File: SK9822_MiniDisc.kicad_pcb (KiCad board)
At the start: 4 copper layers, 220 x 220 mm, 341 parts, among them P1 CONN_01X04, P2 CONN_01X04

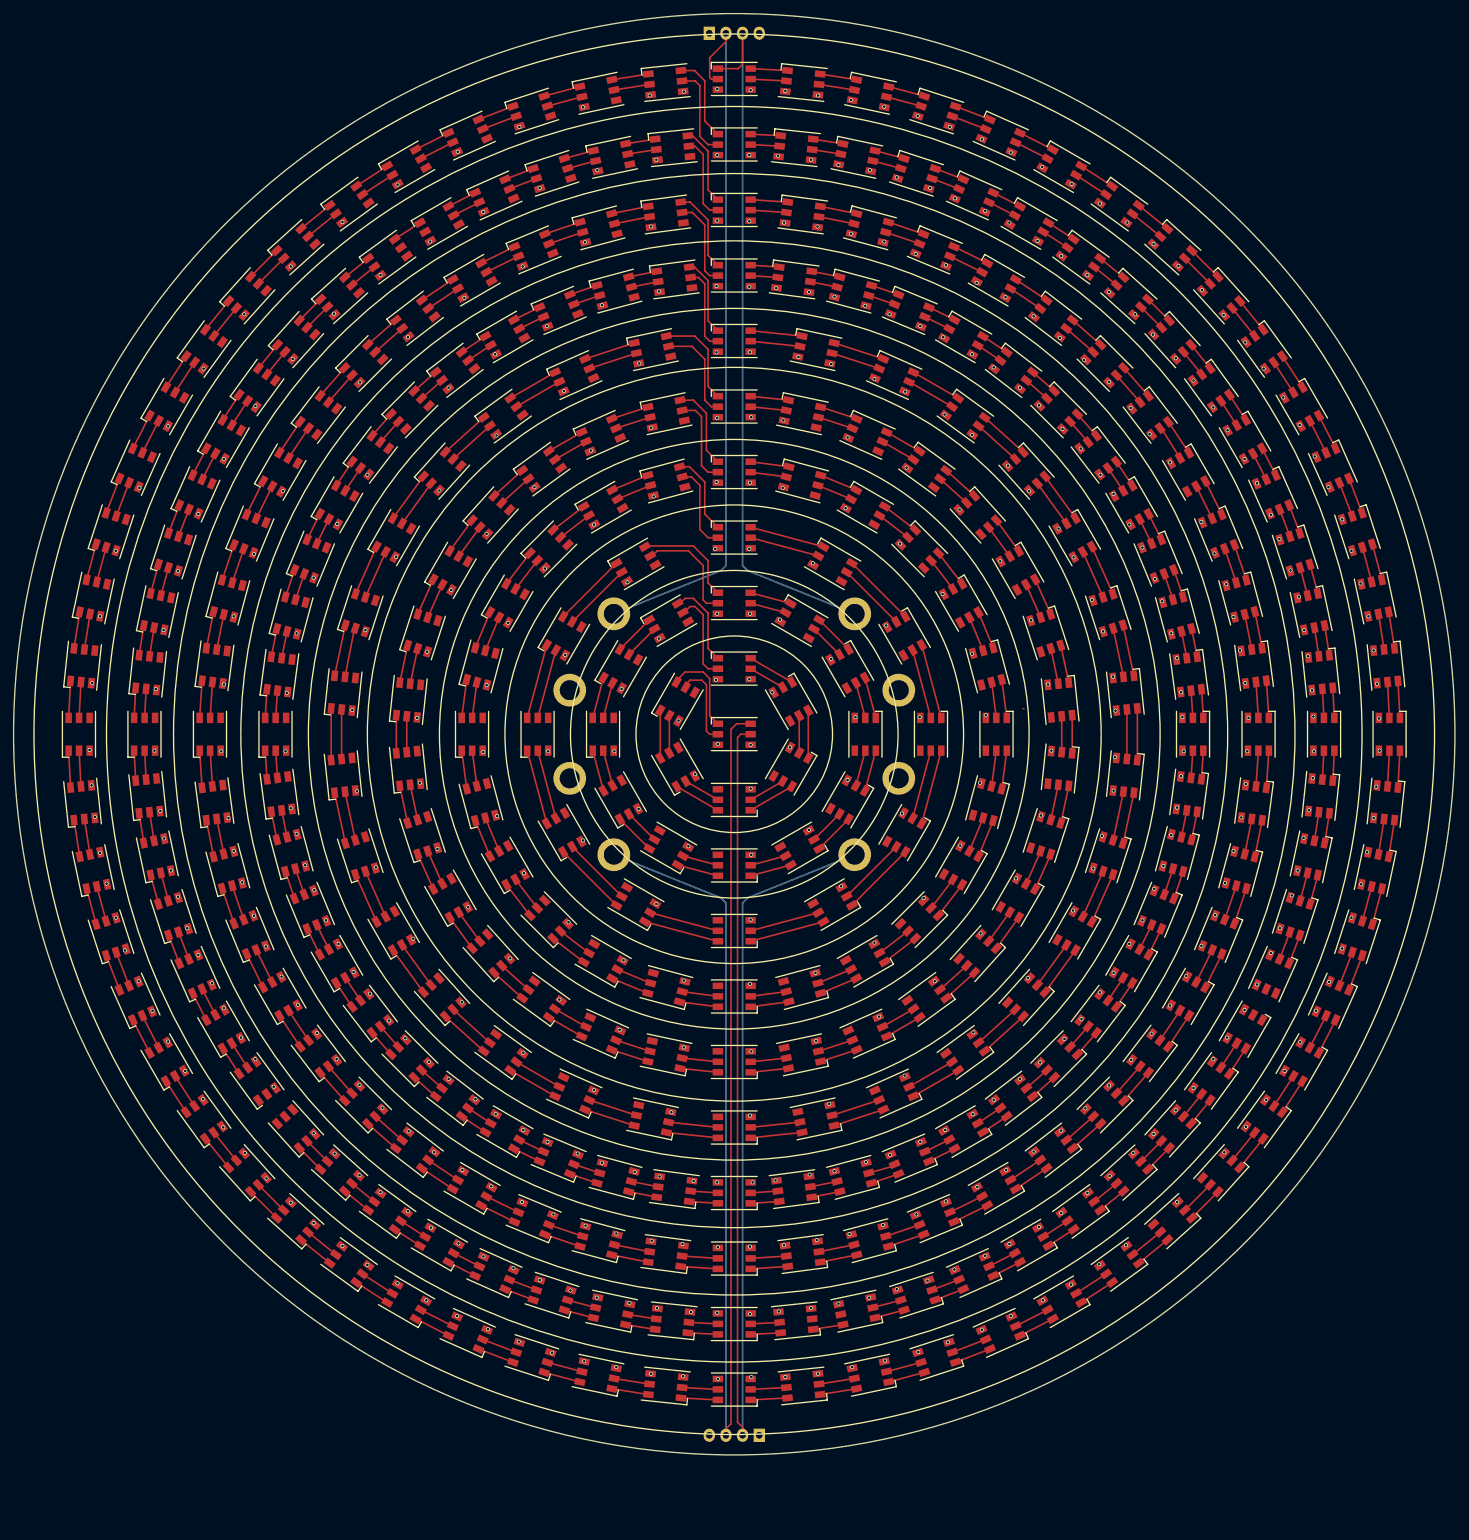
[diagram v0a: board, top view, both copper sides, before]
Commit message: full gnd layout
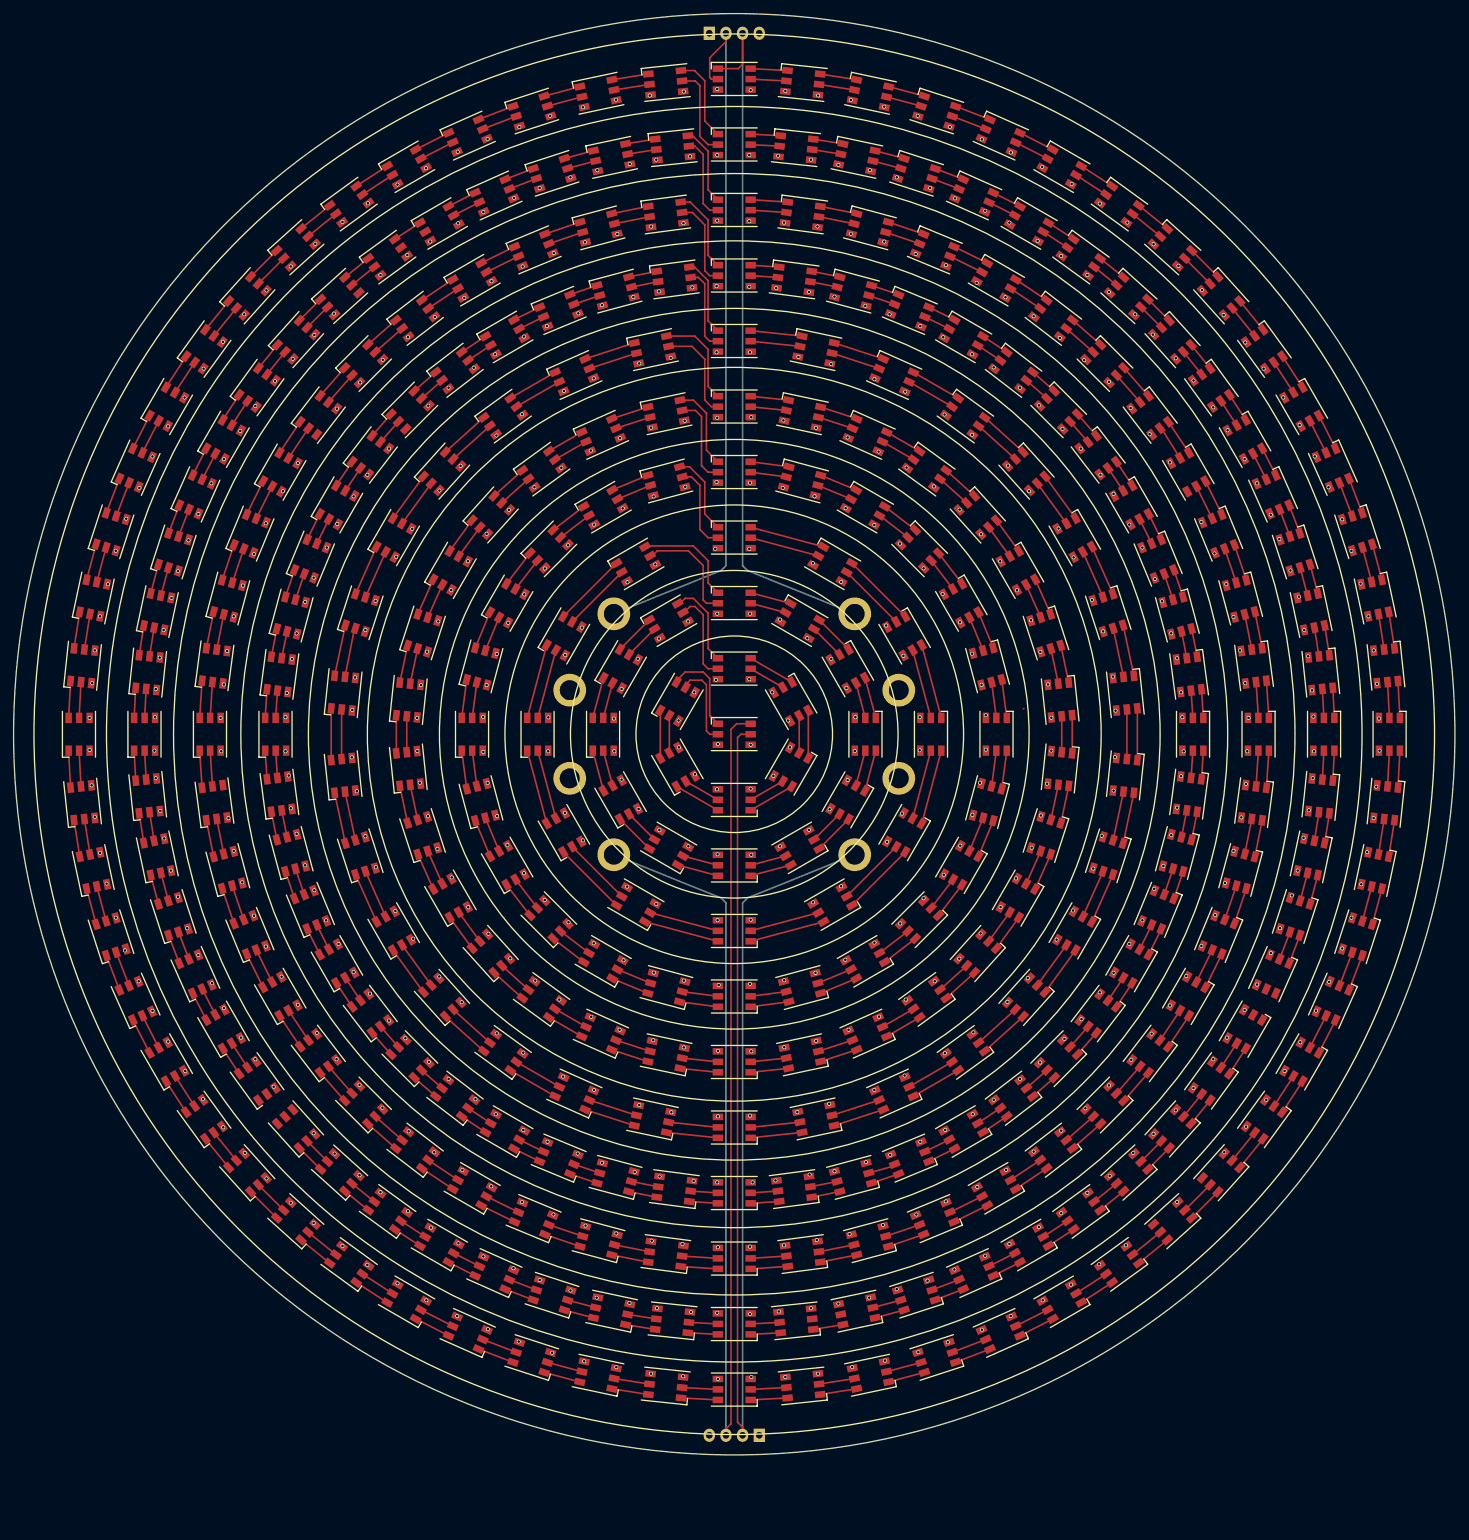
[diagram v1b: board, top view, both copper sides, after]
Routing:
- net VCC: track 3179.4 -> 4018.1 mm, vias 173 -> 326

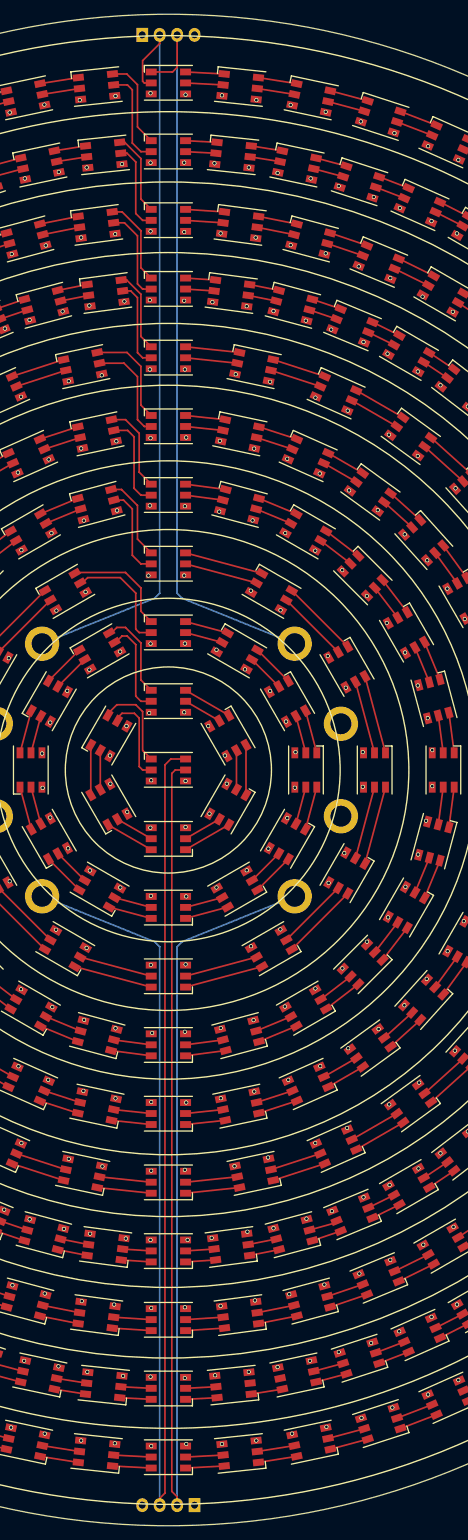
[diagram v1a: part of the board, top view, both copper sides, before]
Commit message: adding caps
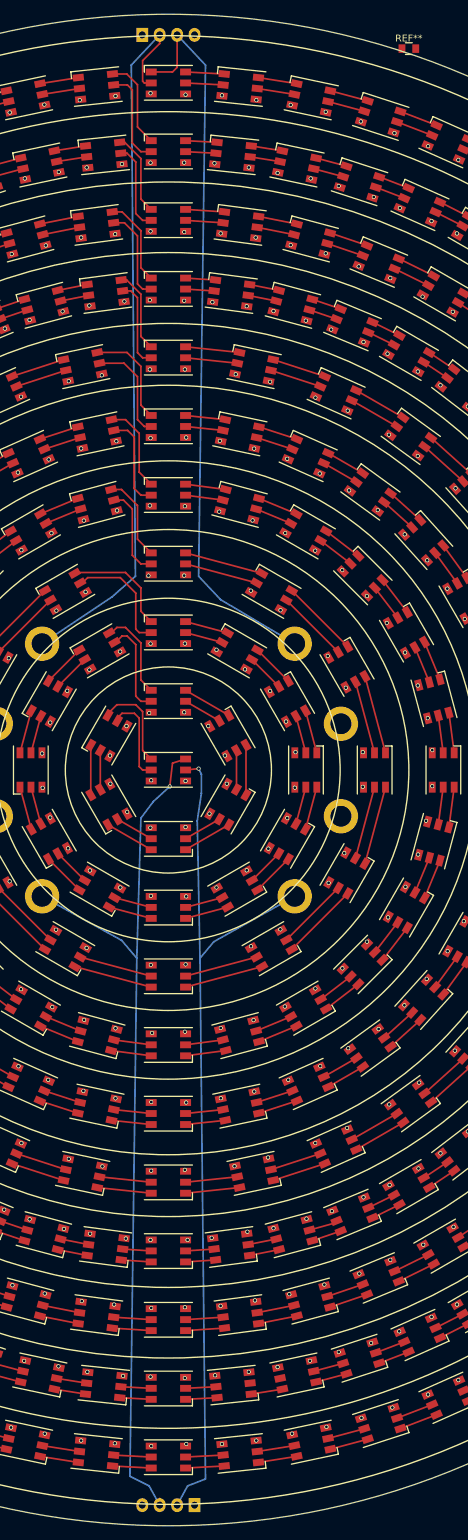
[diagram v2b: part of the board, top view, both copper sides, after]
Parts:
- added REF**: C_0805, Capacitors_SMD:C_0805, F.Cu at (335.0, 95.0)
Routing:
- net Net-(D331-Pad5): track 209.5 -> 128.6 mm, vias 0 -> 1
- net Net-(D331-Pad6): track 212.1 -> 132.2 mm, vias 0 -> 1
- net Net-(D1-Pad2): track 109.1 -> 106.4 mm
- net Net-(D1-Pad1): track 109.5 -> 107.2 mm
